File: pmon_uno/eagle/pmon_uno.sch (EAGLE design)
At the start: 42 parts, among them J1 USB, J2 USB, J3 PINHD-1X3, J4 PINHD-2X3, Q1 16Mhz, U1 LTC2943, U2 FT232RL, U3 LT1764AEQ, U4 ATMEGA328TQFP32

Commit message: Updated schematic and board for rev c.
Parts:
- added J5: PINHD-1X3, pmon_uno:PINHD-1X3
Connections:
- new net N$5: J1.VBUS, J5.3
- net +5V: now also J5.1
- net N$9: now also J5.2; no longer J1.VBUS
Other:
- note added: "POWER SELECTOR"
- moved on the sheet: J1
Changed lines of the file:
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@@
 <part name="S1" library="pmon_uno" deviceset="PUSH_BUTTON_SHIELDED" device=""/>
 <part name="J3" library="pmon_uno" deviceset="PINHD-1X3" device="" value="PINHD-1X3"/>
+<part name="J5" library="pmon_uno" deviceset="PINHD-1X3" device="" value="PINHD-1X3"/>
+<part name="P+6" library="pmon_uno" deviceset="+5V" device=""/>
 </parts>
 <sheets>
@@
 <text x="12.7" y="104.14" size="2.54" layer="97">C/V/A SENSE</text>
 <text x="38.1" y="167.64" size="2.54" layer="97">VOLTAGE REGULATOR</text>
-<text x="-20.32" y="187.96" size="2.54" layer="97">FROM
+<text x="-20.32" y="180.34" size="2.54" layer="97">FROM
 CHARGER</text>
 <text x="93.98" y="104.14" size="2.54" layer="97">LOGIC ANALYZER *</text>
@@
 <text x="180.34" y="139.7" size="2.54" layer="97">"ARDUINO MINI PRO 328P 5V 16Mhz"</text>
 <text x="152.654" y="104.14" size="2.54" layer="97">START</text>
+<text x="-14.732" y="218.186" size="2.54" layer="97">POWER
+SELECTOR</text>
 </plain>
 <instances>
@@
 <instance part="GND19" gate="1" x="48.26" y="185.42"/>
 <instance part="GND20" gate="1" x="43.18" y="185.42"/>
-<instance part="GND21" gate="1" x="5.08" y="185.42"/>
+<instance part="GND21" gate="1" x="7.62" y="185.42"/>
 <instance part="R6" gate="G$1" x="109.22" y="200.66" smashed="yes" rot="R180">
 <attribute name="NAME" x="110.49" y="198.9074" size="1.778" layer="95" rot="R180"/>
@@
 <instance part="S2" gate="G$1" x="177.8" y="119.38" rot="R270"/>
 <instance part="GND30" gate="1" x="167.64" y="109.22"/>
-<instance part="J1" gate="G$1" x="-5.08" y="200.66"/>
+<instance part="J1" gate="G$1" x="-7.62" y="193.04"/>
 <instance part="R5" gate="G$1" x="101.6" y="190.5" smashed="yes" rot="MR0">
 <attribute name="NAME" x="104.14" y="193.04" size="1.778" layer="95" rot="MR90"/>
@@
 <instance part="U$4" gate="G$1" x="68.58" y="53.34" rot="R180"/>
 <instance part="U$6" gate="G$1" x="68.58" y="50.8" rot="R180"/>
-<instance part="U$2" gate="G$1" x="2.54" y="208.28" rot="R180"/>
-<instance part="U$7" gate="G$1" x="2.54" y="205.74" rot="R180"/>
-<instance part="U$8" gate="G$1" x="2.54" y="203.2" rot="R180"/>
+<instance part="U$2" gate="G$1" x="0" y="200.66" rot="R180"/>
+<instance part="U$7" gate="G$1" x="0" y="198.12" rot="R180"/>
+<instance part="U$8" gate="G$1" x="0" y="195.58" rot="R180"/>
 <instance part="U$9" gate="G$1" x="238.76" y="162.56" rot="R180"/>
 <instance part="S1" gate="G$1" x="157.48" y="119.38" smashed="yes">
@@
 </instance>
 <instance part="J3" gate="A" x="132.08" y="190.5"/>
+<instance part="J5" gate="A" x="5.08" y="210.82" smashed="yes" rot="MR0">
+<attribute name="NAME" x="13.208" y="213.995" size="1.778" layer="95" rot="MR180"/>
+<attribute name="VALUE" x="13.716" y="217.424" size="1.778" layer="96" rot="MR180"/>
+</instance>
+<instance part="P+6" gate="1" x="7.62" y="220.98" smashed="yes">
+<attribute name="VALUE" x="10.668" y="219.456" size="1.778" layer="96" rot="R90"/>
+</instance>
 </instances>
 <busses>
@@
 </segment>
 <segment>
-<wire x1="2.54" y1="200.66" x2="5.08" y2="200.66" width="0.4064" layer="91"/>
-<wire x1="5.08" y1="200.66" x2="5.08" y2="187.96" width="0.4064" layer="91"/>
+<wire x1="0" y1="193.04" x2="7.62" y2="193.04" width="0.4064" layer="91"/>
+<wire x1="7.62" y1="193.04" x2="7.62" y2="187.96" width="0.4064" layer="91"/>
 <pinref part="GND21" gate="1" pin="GND"/>
 <pinref part="J1" gate="G$1" pin="GND"/>
@@
 <pinref part="P+4" gate="1" pin="+5V"/>
 </segment>
+<segment>
+<pinref part="J5" gate="A" pin="1"/>
+<pinref part="P+6" gate="1" pin="+5V"/>
+<wire x1="7.62" y1="213.36" x2="7.62" y2="218.44" width="0.4064" layer="91"/>
+</segment>
 </net>
 <net name="ERROR_LED" class="0">
@@
 <junction x="33.02" y="210.82"/>
 <junction x="25.4" y="210.82"/>
-<pinref part="J1" gate="G$1" pin="VBUS"/>
-<wire x1="2.54" y1="210.82" x2="17.78" y2="210.82" width="0.4064" layer="91"/>
+<pinref part="J5" gate="A" pin="2"/>
+<wire x1="7.62" y1="210.82" x2="17.78" y2="210.82" width="0.4064" layer="91"/>
 <junction x="17.78" y="210.82"/>
 </segment>
@@
 </segment>
 </net>
+<net name="N$5" class="0">
+<segment>
+<pinref part="J1" gate="G$1" pin="VBUS"/>
+<pinref part="J5" gate="A" pin="3"/>
+<wire x1="0" y1="203.2" x2="7.62" y2="203.2" width="0.4064" layer="91"/>
+<wire x1="7.62" y1="203.2" x2="7.62" y2="208.28" width="0.4064" layer="91"/>
+</segment>
+</net>

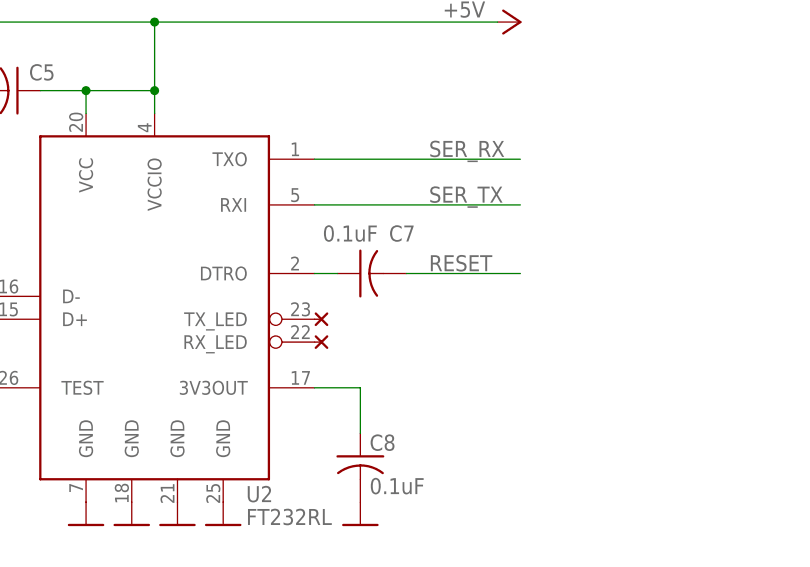
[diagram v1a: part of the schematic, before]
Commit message: Increased the dril of the USB connector two main support tabs.
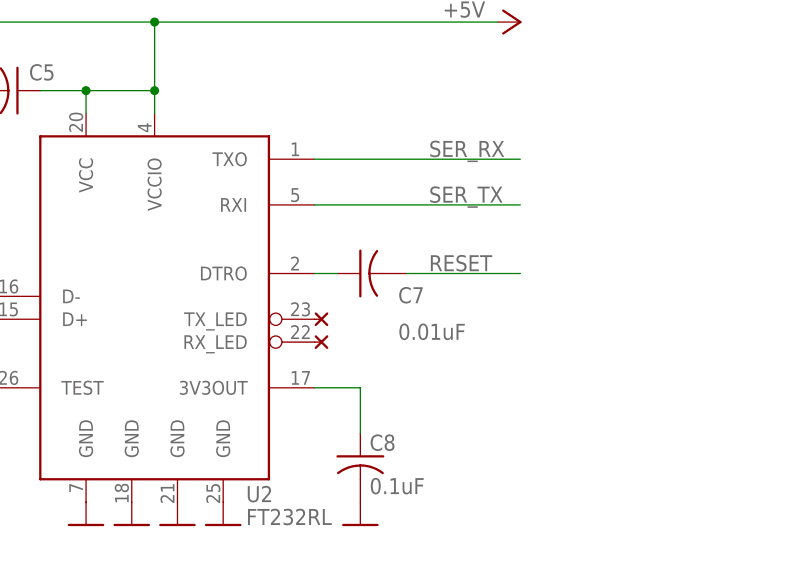
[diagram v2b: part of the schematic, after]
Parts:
- C7: value 0.1uF -> 0.01uF
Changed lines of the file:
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@@
 <part name="R10" library="pmon_uno" deviceset="RES-" device="R0603" value="3.3K"/>
 <part name="GND3" library="pmon_uno" deviceset="GND" device=""/>
-<part name="C7" library="pmon_uno" deviceset="CAP-" device="C0603" value="0.1uF"/>
+<part name="C7" library="pmon_uno" deviceset="CAP-" device="C0603" value="0.01uF"/>
 <part name="P+2" library="pmon_uno" deviceset="+5V" device=""/>
 <part name="GND2" library="pmon_uno" deviceset="GND" device=""/>
@@
 <instance part="GND3" gate="1" x="193.04" y="55.88"/>
 <instance part="C7" gate="G$1" x="73.66" y="58.42" smashed="yes" rot="R90">
-<attribute name="NAME" x="76.835" y="61.976" size="1.778" layer="95"/>
-<attribute name="VALUE" x="69.469" y="61.976" size="1.778" layer="96"/>
+<attribute name="NAME" x="77.851" y="55.118" size="1.778" layer="95"/>
+<attribute name="VALUE" x="77.851" y="51.054" size="1.778" layer="96"/>
 </instance>
 <instance part="P+2" gate="1" x="187.96" y="220.98"/>

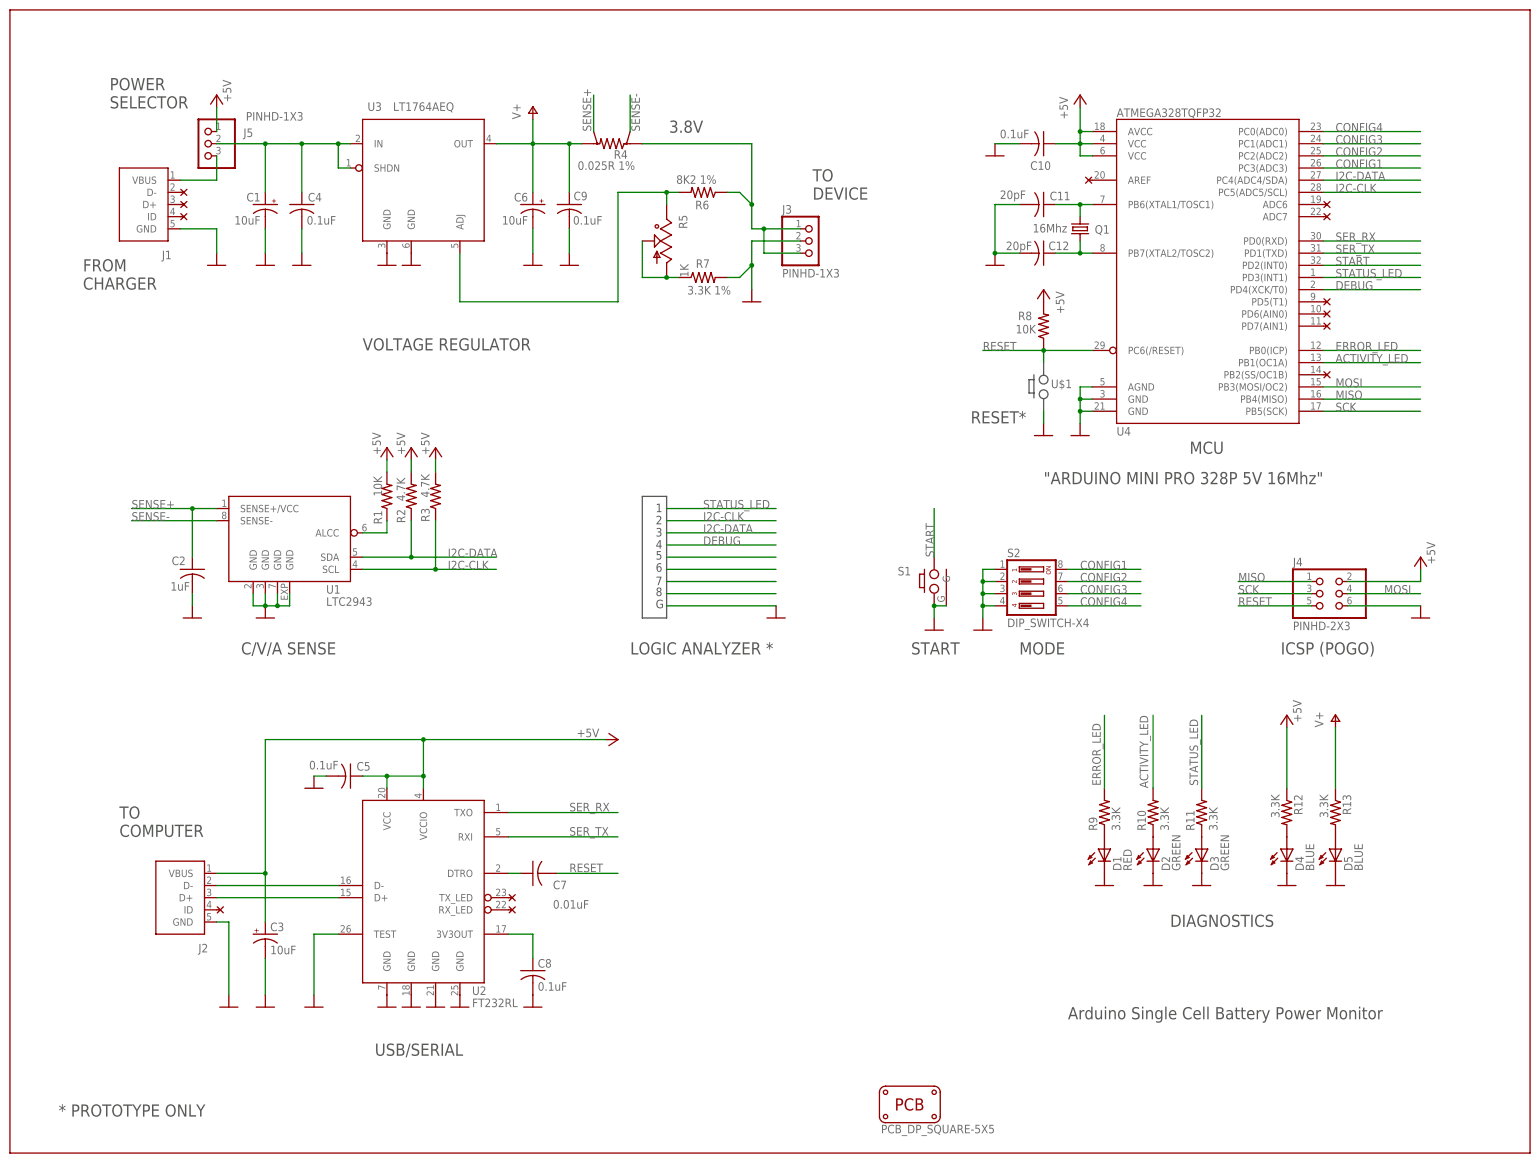
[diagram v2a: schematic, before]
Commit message: Changed resistor values to reduce part SKU count. Selected different 1% resistor since the old ones did not have readable markings.
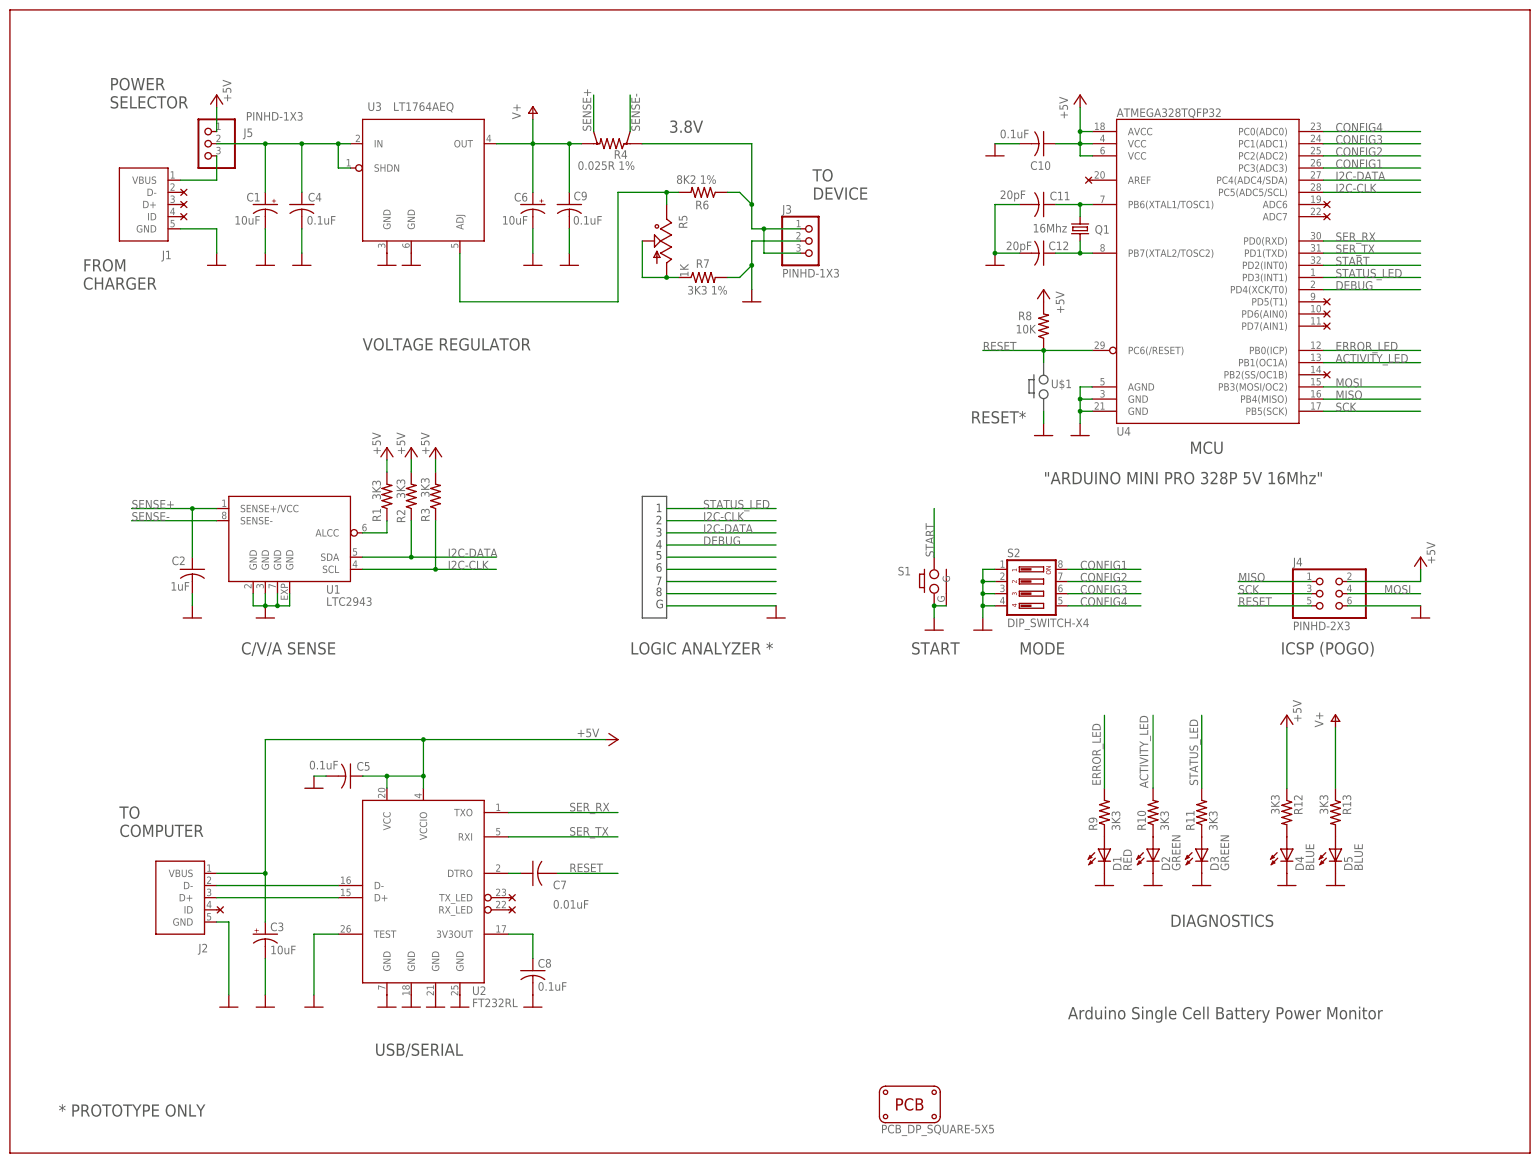
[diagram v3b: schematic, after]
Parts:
- R1: value 10K -> 3K3
- R10, R11, R12, R13, R9: value 3.3K -> 3K3
- R2, R3: value 4.7K -> 3K3
- R7: value 3.3K 1% -> 3K3 1%
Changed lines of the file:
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@@
 </classes>
 <parts>
-<part name="R9" library="pmon_uno" deviceset="RES-" device="R0603" value="3.3K"/>
-<part name="R10" library="pmon_uno" deviceset="RES-" device="R0603" value="3.3K"/>
+<part name="R9" library="pmon_uno" deviceset="RES-" device="R0603" value="3K3"/>
+<part name="R10" library="pmon_uno" deviceset="RES-" device="R0603" value="3K3"/>
 <part name="GND3" library="pmon_uno" deviceset="GND" device=""/>
 <part name="C7" library="pmon_uno" deviceset="CAP-" device="C0603" value="0.01uF"/>
@@
 <part name="GND1" library="pmon_uno" deviceset="GND" device=""/>
 <part name="D4" library="pmon_uno" deviceset="LED" device="1206" value="BLUE"/>
-<part name="R12" library="pmon_uno" deviceset="RES-" device="R0603" value="3.3K"/>
+<part name="R12" library="pmon_uno" deviceset="RES-" device="R0603" value="3K3"/>
 <part name="P+4" library="pmon_uno" deviceset="+5V" device=""/>
 <part name="C8" library="pmon_uno" deviceset="CAP-" device="C0603" value="0.1uF"/>
@@
 <part name="GND21" library="pmon_uno" deviceset="GND" device=""/>
 <part name="R6" library="pmon_uno" deviceset="RES-" device="R0603" value="8K2 1%"/>
-<part name="R7" library="pmon_uno" deviceset="RES-" device="R0603" value="3.3K 1%"/>
+<part name="R7" library="pmon_uno" deviceset="RES-" device="R0603" value="3K3 1%"/>
 <part name="GND23" library="pmon_uno" deviceset="GND" device=""/>
 <part name="C6" library="pmon_uno" deviceset="CPOL-US" device="A/3216-18R" value="10uF"/>
@@
 <part name="P+9" library="pmon_uno" deviceset="V+" device=""/>
 <part name="R4" library="pmon_uno" deviceset="RES-SHUNT-" device="6432" value="0.025R 1%"/>
-<part name="R2" library="pmon_uno" deviceset="RES-" device="R0603" value="4.7K"/>
-<part name="R3" library="pmon_uno" deviceset="RES-" device="R0603" value="4.7K"/>
+<part name="R2" library="pmon_uno" deviceset="RES-" device="R0603" value="3K3"/>
+<part name="R3" library="pmon_uno" deviceset="RES-" device="R0603" value="3K3"/>
 <part name="P+11" library="pmon_uno" deviceset="+5V" device=""/>
 <part name="P+12" library="pmon_uno" deviceset="+5V" device=""/>
@@
 <part name="GND17" library="pmon_uno" deviceset="GND" device=""/>
 <part name="D5" library="pmon_uno" deviceset="LED" device="1206" value="BLUE"/>
-<part name="R13" library="pmon_uno" deviceset="RES-" device="R0603" value="3.3K"/>
+<part name="R13" library="pmon_uno" deviceset="RES-" device="R0603" value="3K3"/>
 <part name="GND28" library="pmon_uno" deviceset="GND" device=""/>
 <part name="P+8" library="pmon_uno" deviceset="V+" device=""/>
 <part name="GND31" library="pmon_uno" deviceset="GND" device=""/>
-<part name="R1" library="pmon_uno" deviceset="RES-" device="R0603" value="10K"/>
+<part name="R1" library="pmon_uno" deviceset="RES-" device="R0603" value="3K3"/>
 <part name="P+10" library="pmon_uno" deviceset="+5V" device=""/>
 <part name="D3" library="pmon_uno" deviceset="LED" device="1206" value="GREEN"/>
 <part name="GND32" library="pmon_uno" deviceset="GND" device=""/>
-<part name="R11" library="pmon_uno" deviceset="RES-" device="R0603" value="3.3K"/>
+<part name="R11" library="pmon_uno" deviceset="RES-" device="R0603" value="3K3"/>
 <part name="GND22" library="pmon_uno" deviceset="GND" device=""/>
 <part name="J2" library="pmon_uno" deviceset="USB" device=""/>
@@
 <instance part="R2" gate="G$1" x="48.26" y="137.16" smashed="yes" rot="R90">
 <attribute name="NAME" x="47.0154" y="131.572" size="1.778" layer="95" rot="R90"/>
-<attribute name="VALUE" x="46.99" y="136.144" size="1.778" layer="96" rot="R90"/>
+<attribute name="VALUE" x="46.99" y="136.652" size="1.778" layer="96" rot="R90"/>
 </instance>
 <instance part="R3" gate="G$1" x="53.34" y="137.16" smashed="yes" rot="R90">
@@
 <instance part="GND31" gate="1" x="180.34" y="149.86"/>
 <instance part="R1" gate="G$1" x="43.18" y="137.16" smashed="yes" rot="R90">
-<attribute name="NAME" x="42.1894" y="131.318" size="1.778" layer="95" rot="R90"/>
-<attribute name="VALUE" x="42.164" y="137.16" size="1.778" layer="96" rot="R90"/>
+<attribute name="NAME" x="41.9354" y="131.826" size="1.778" layer="95" rot="R90"/>
+<attribute name="VALUE" x="41.91" y="136.398" size="1.778" layer="96" rot="R90"/>
 </instance>
 <instance part="P+10" gate="1" x="43.18" y="147.32" smashed="yes" rot="MR0">

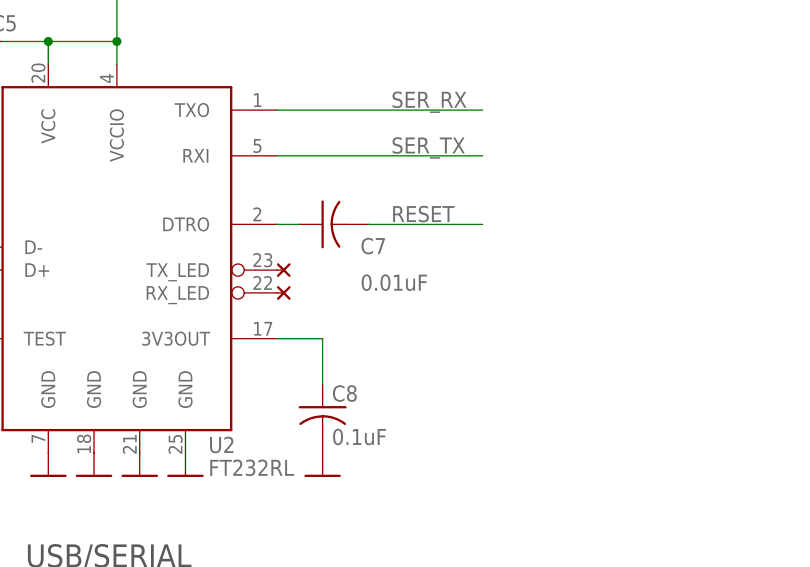
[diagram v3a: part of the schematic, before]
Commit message: Changed reset capacitor from 0.01 to 0.1 (to reduce compoent kind count).
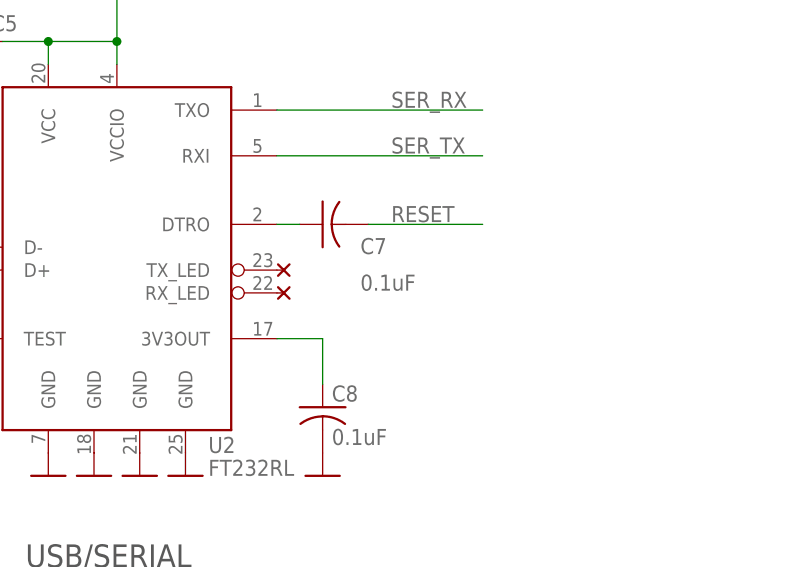
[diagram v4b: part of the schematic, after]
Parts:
- C7: value 0.01uF -> 0.1uF
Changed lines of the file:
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@@
 <part name="R10" library="pmon_uno" deviceset="RES-" device="R0603" value="3K3"/>
 <part name="GND3" library="pmon_uno" deviceset="GND" device=""/>
-<part name="C7" library="pmon_uno" deviceset="CAP-" device="C0603" value="0.01uF"/>
+<part name="C7" library="pmon_uno" deviceset="CAP-" device="C0603" value="0.1uF"/>
 <part name="P+2" library="pmon_uno" deviceset="+5V" device=""/>
 <part name="GND2" library="pmon_uno" deviceset="GND" device=""/>
